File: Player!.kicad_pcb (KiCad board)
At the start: 2 copper layers, 95.2 x 38.1 mm, 25 parts, among them J1 USB4085-GF-A_REVA4, SW1 RotaryEncoder_Switch, SW2 SW_Push, SW3 SW_Push, SW4 SW_Push, SW5 SW_Push, Y1 Crystal

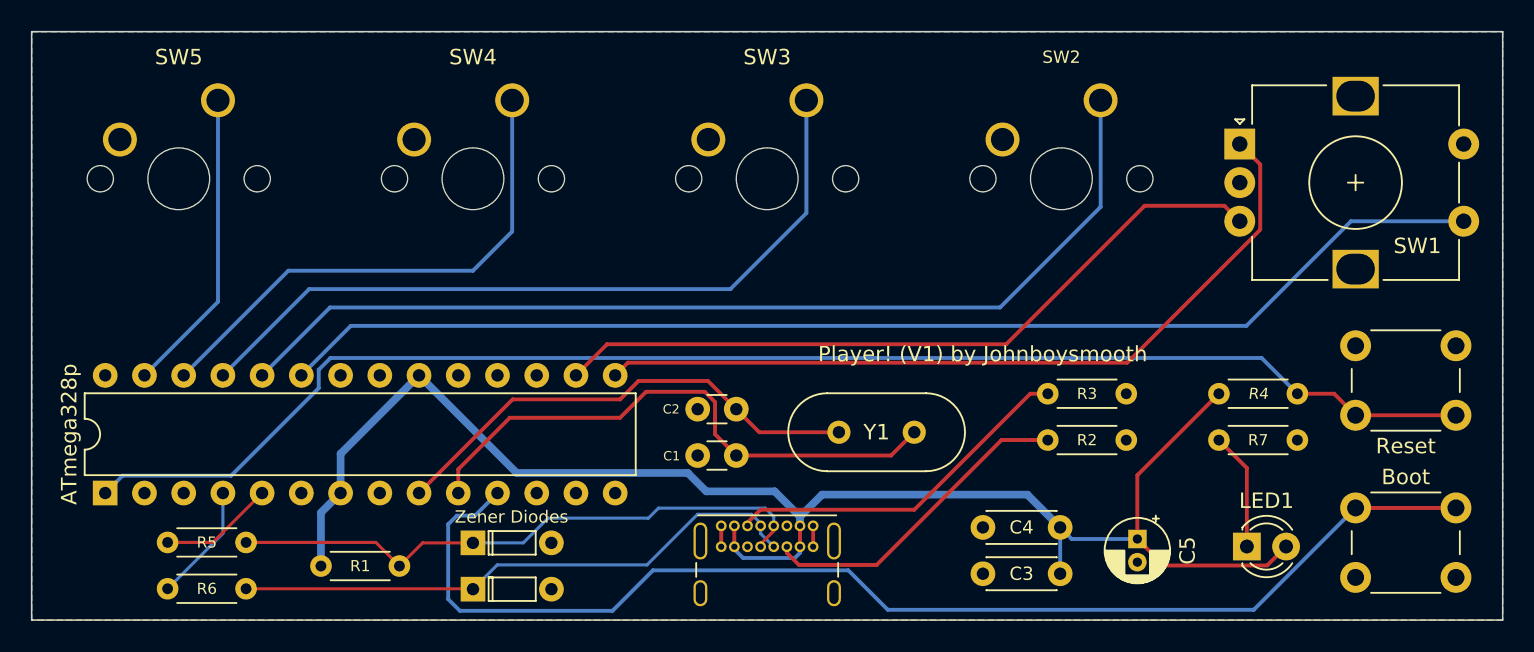
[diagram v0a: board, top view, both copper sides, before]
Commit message: Minor Changes for V1.1
Altered encoder location, some minor changes to front silkscreen texts
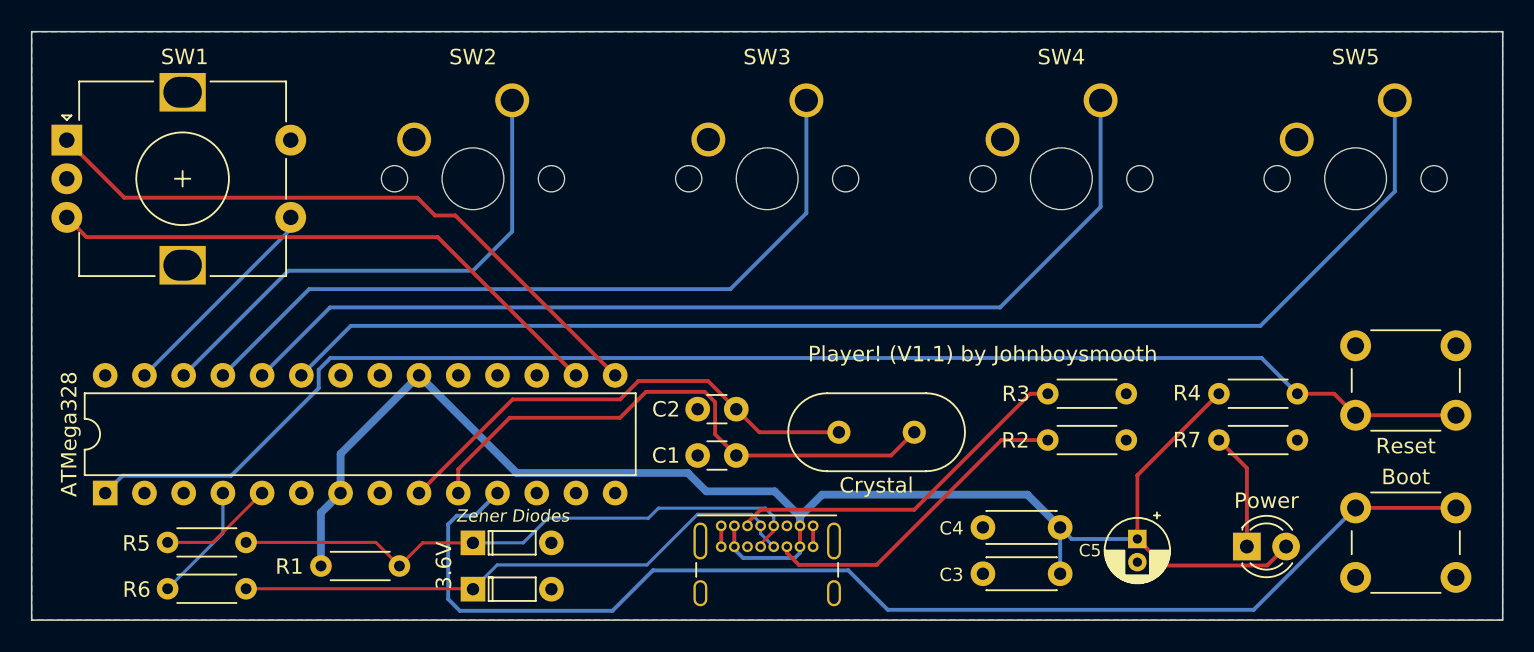
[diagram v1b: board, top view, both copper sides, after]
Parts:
- moved SW5 76.2 mm to (88.3, 4.45)
- moved SW1 76.0 mm to (2.27, 7.03)
- renumbered ATmega328p to ATMega328, LED1 to Power, SW4 to SW2, SW2 to SW4
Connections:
- ATMega328 pad 23: SW1 -> SW5
- ATMega328 pad 24: SW2 -> SW4
- ATMega328 pad 26: SW4 -> SW2
- ATMega328 pad 27: SW5 -> SW1
- SW2 pad 1: SW4 -> SW2
- SW4 pad 1: SW2 -> SW4
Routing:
- net SW1: track 79.4 -> 14.2 mm
- net SW5: track 19.8 -> 81.6 mm
- net SW4: track 33.6 -> 65.7 mm
- net SW2: track 65.7 -> 33.6 mm
- net ROTB: track 47.9 -> 37.2 mm
- net ROTA: track 51.8 -> 41.8 mm
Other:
- board text added: "3.6V"
- board text added: "Player! (V1.1) by Johnboysmooth"
- board text removed: "Player! (V1) by Johnboysmooth"

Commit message: 3D Models
Added models missing for various components, rotated PCB and text. Updated readme with images
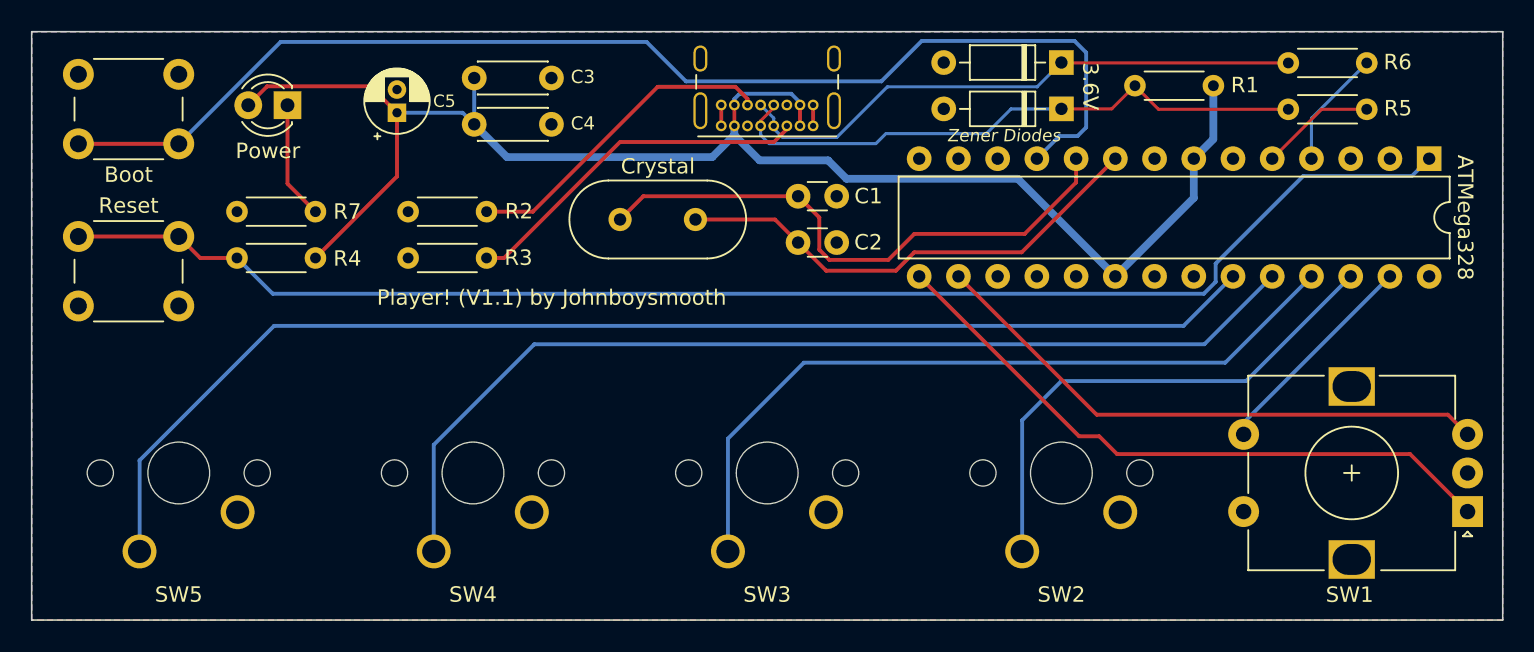
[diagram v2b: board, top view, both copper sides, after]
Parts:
- DN1, DP1: footprint Keyboard Stuff:D_DO-35_SOD27_P5.08mm_Vertical_AnodeUp -> Keyboard Stuff:D_DO-35_SOD27_P7.62mm_Horizontal
- moved SW1 93.8 mm to (93.0, 31.1), turned to 180 degrees
- moved Reset 89.9 mm to (3.02, 13.3), turned to 0 degrees
- moved ATMega328 88.4 mm to (90.5, 8.22), turned to -90 degrees
- moved SW5 86.4 mm to (6.99, 33.7), turned to 180 degrees
- moved Boot 79.8 mm to (9.53, 7.26), turned to 180 degrees
- moved R6 75.6 mm to (81.4, 2.03), turned to 0 degrees
- moved R5 73.1 mm to (81.4, 5.03), turned to 0 degrees
- moved R7 70.2 mm to (13.3, 11.7), turned to 0 degrees
- moved Power 68.4 mm to (16.6, 4.76), turned to 180 degrees
- moved R1 65.6 mm to (76.5, 3.50), turned to 180 degrees
- moved R4 59.2 mm to (18.4, 14.7), turned to 180 degrees
- moved C5 55.3 mm to (23.7, 5.25), turned to 90 degrees
- moved SW4 52.1 mm to (26.0, 33.7), turned to 180 degrees
- moved DN1 51.1 mm to (66.7, 2.00), turned to 180 degrees
- moved C3 49.7 mm to (28.7, 3.00), turned to 0 degrees
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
